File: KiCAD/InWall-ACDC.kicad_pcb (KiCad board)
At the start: 2 copper layers, 51 x 36 mm, 64 parts, among them J1 Screw_Terminal_01x02, J2 Conn_01x03, U1 HLK-PM03, U2 DS18B20

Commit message: local lib: holes 0.5, 1mm
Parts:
- REF** (x51): footprint lib_projet:hole_1mm -> Project_Module:hole_1mm
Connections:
- J2 pad 1: +3V3 -> GND
- J2 pad 3: GND -> +3V3
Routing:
- net +3V3: track 40.9 -> 34.6 mm
- net Net-(J2-Pad2): track 18.0 -> 12.1 mm
- net GND: track 59.5 -> 57.8 mm

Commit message: logo
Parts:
- added G***: LOGO, Project_Module:logo_marsu31_L5mm_H6mm, B.Cu at (173.6, 80.2)
- moved REF** 1.22 mm to (202.9, 80.9)
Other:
- board text removed: "MIT License"

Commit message: allègement logo
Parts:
- moved G*** 0.73 mm to (173.8, 80.9)

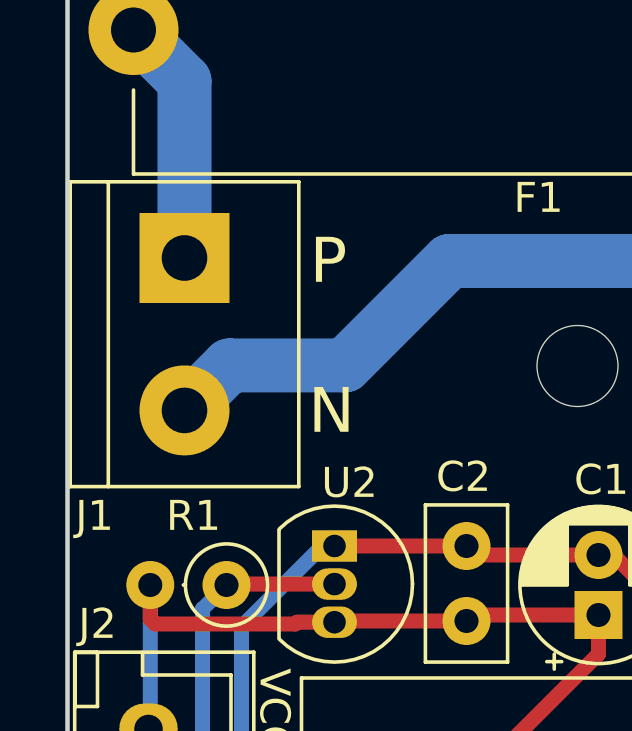
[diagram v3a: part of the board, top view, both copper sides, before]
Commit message: ajout modele 3D bornier + màj gerber
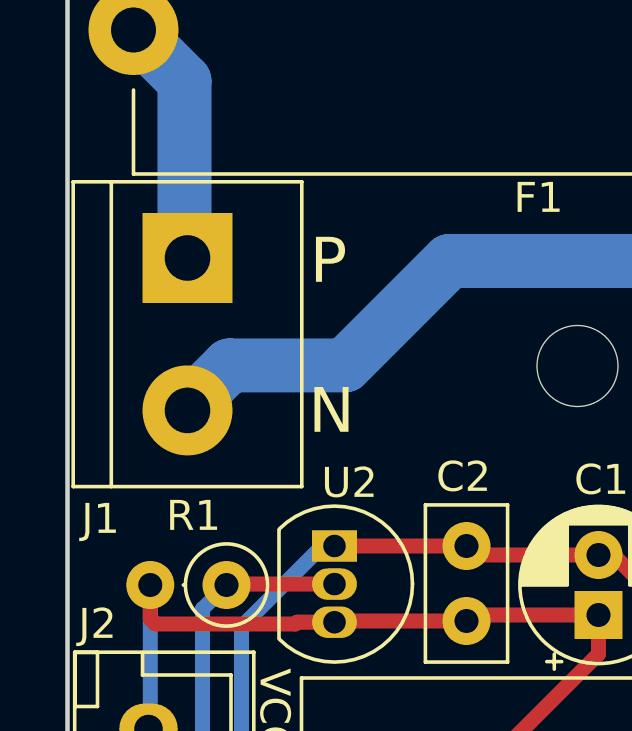
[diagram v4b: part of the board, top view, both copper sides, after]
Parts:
- J1: footprint TerminalBlock:TerminalBlock_bornier-2_P5.08mm -> Project_Module:TerminalBlock_bornier-2_P5.08mm
- moved J1 0.10 mm to (166.0, 61.4)
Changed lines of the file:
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@@
-(kicad_pcb (version 20171130) (host pcbnew 5.1.2-f72e74a~84~ubuntu18.04.1)
+(kicad_pcb (version 20171130) (host pcbnew 5.1.3-ffb9f22~84~ubuntu18.04.1)
   (general
     (thickness 1.6)
@@
       (usegerberattributes true)
       (usegerberadvancedattributes false)
-      (creategerberjobfile false)
+      (creategerberjobfile true)
       (excludeedgelayer true)
       (linewidth 0.100000)
@@
     (add_net "Net-(F1-Pad1)")
     (add_net "Net-(F1-Pad2)")
+  )
+  (module Project_Module:TerminalBlock_bornier-2_P5.08mm (layer F.Cu)
+    (at 166 61.4 270)
+    (descr "simple 2-pin terminal block, pitch 5.08mm, revamped version of bornier2")
+    (tags "terminal block bornier2")
+    (fp_text reference J1 (at 8.7 2.9 180) (layer F.SilkS)
+      (effects (font (size 1 1) (thickness 0.15)))
+    )
+    (fp_text value Screw_Terminal_01x02 (at 2.54 5.08 90) (layer F.Fab)
+      (effects (font (size 1 1) (thickness 0.15)))
+    )
+    (fp_line (start 7.79 4) (end -2.71 4) (layer F.CrtYd) (width 0.05))
+    (fp_line (start 7.79 4) (end 7.79 -4) (layer F.CrtYd) (width 0.05))
+    (fp_line (start -2.71 -4) (end -2.71 4) (layer F.CrtYd) (width 0.05))
+    (fp_line (start -2.71 -4) (end 7.79 -4) (layer F.CrtYd) (width 0.05))
+    (fp_line (start -2.54 3.81) (end 7.62 3.81) (layer F.SilkS) (width 0.12))
+    (fp_line (start -2.54 -3.81) (end -2.54 3.81) (layer F.SilkS) (width 0.12))
+    (fp_line (start 7.62 -3.81) (end -2.54 -3.81) (layer F.SilkS) (width 0.12))
+    (fp_line (start 7.62 3.81) (end 7.62 -3.81) (layer F.SilkS) (width 0.12))
+    (fp_line (start 7.62 2.54) (end -2.54 2.54) (layer F.SilkS) (width 0.12))
+    (fp_line (start 7.54 -3.75) (end -2.46 -3.75) (layer F.Fab) (width 0.1))
+    (fp_line (start 7.54 3.75) (end 7.54 -3.75) (layer F.Fab) (width 0.1))
+    (fp_line (start -2.46 3.75) (end 7.54 3.75) (layer F.Fab) (width 0.1))
+    (fp_line (start -2.46 -3.75) (end -2.46 3.75) (layer F.Fab) (width 0.1))
+    (fp_line (start -2.41 2.55) (end 7.49 2.55) (layer F.Fab) (width 0.1))
+    (fp_text user %R (at 2.54 0 90) (layer F.Fab)
+      (effects (font (size 1 1) (thickness 0.15)))
+    )
+    (pad 2 thru_hole circle (at 5.08 0 270) (size 3 3) (drill 1.52) (layers *.Cu *.Mask)
+      (net 4 NEUT))
+    (pad 1 thru_hole rect (at 0 0 270) (size 3 3) (drill 1.52) (layers *.Cu *.Mask)
+      (net 2 "Net-(F1-Pad2)"))
+    (model ${KISYS3DMOD}/TerminalBlock.3dshapes/TerminalBlock_bornier-2_P5.08mm.wrl
+      (offset (xyz 2.54 0 0))
+      (scale (xyz 1 1 1))
+      (rotate (xyz 0 0 0))
+    )
+    (model ${KIPRJMOD}/project_module.pretty/screw_terminal_01x02_P5_08mm.step
+      (offset (xyz 2.5 0 0))
+      (scale (xyz 1 1 1))
+      (rotate (xyz 0 0 -90))
+    )
   )
   (module Project_Module:logo_marsu31_L5mm_H6mm (layer B.Cu)
@@
       (scale (xyz 1 1 1))
       (rotate (xyz 0 0 0))
-    )
-  )
-  (module TerminalBlock:TerminalBlock_bornier-2_P5.08mm (layer F.Cu)
-    (at 165.9 61.4 270)
-    (descr "simple 2-pin terminal block, pitch 5.08mm, revamped version of bornier2")
-    (tags "terminal block bornier2")
-    (fp_text reference J1 (at 8.6 3 180) (layer F.SilkS)
-      (effects (font (size 1 1) (thickness 0.15)))
-    )
-    (fp_text value Screw_Terminal_01x02 (at 2.54 5.08 90) (layer F.Fab)
-      (effects (font (size 1 1) (thickness 0.15)))
-    )
-    (fp_line (start 7.79 4) (end -2.71 4) (layer F.CrtYd) (width 0.05))
-    (fp_line (start 7.79 4) (end 7.79 -4) (layer F.CrtYd) (width 0.05))
-    (fp_line (start -2.71 -4) (end -2.71 4) (layer F.CrtYd) (width 0.05))
-    (fp_line (start -2.71 -4) (end 7.79 -4) (layer F.CrtYd) (width 0.05))
-    (fp_line (start -2.54 3.81) (end 7.62 3.81) (layer F.SilkS) (width 0.12))
-    (fp_line (start -2.54 -3.81) (end -2.54 3.81) (layer F.SilkS) (width 0.12))
-    (fp_line (start 7.62 -3.81) (end -2.54 -3.81) (layer F.SilkS) (width 0.12))
-    (fp_line (start 7.62 3.81) (end 7.62 -3.81) (layer F.SilkS) (width 0.12))
-    (fp_line (start 7.62 2.54) (end -2.54 2.54) (layer F.SilkS) (width 0.12))
-    (fp_line (start 7.54 -3.75) (end -2.46 -3.75) (layer F.Fab) (width 0.1))
-    (fp_line (start 7.54 3.75) (end 7.54 -3.75) (layer F.Fab) (width 0.1))
-    (fp_line (start -2.46 3.75) (end 7.54 3.75) (layer F.Fab) (width 0.1))
-    (fp_line (start -2.46 -3.75) (end -2.46 3.75) (layer F.Fab) (width 0.1))
-    (fp_line (start -2.41 2.55) (end 7.49 2.55) (layer F.Fab) (width 0.1))
-    (fp_text user %R (at 2.54 0 90) (layer F.Fab)
-      (effects (font (size 1 1) (thickness 0.15)))
-    )
-    (pad 2 thru_hole circle (at 5.08 0 270) (size 3 3) (drill 1.52) (layers *.Cu *.Mask)
-      (net 4 NEUT))
-    (pad 1 thru_hole rect (at 0 0 270) (size 3 3) (drill 1.52) (layers *.Cu *.Mask)
-      (net 2 "Net-(F1-Pad2)"))
-    (model ${KISYS3DMOD}/TerminalBlock.3dshapes/TerminalBlock_bornier-2_P5.08mm.wrl
-      (offset (xyz 2.539999961853027 0 0))
-      (scale (xyz 1 1 1))
-      (rotate (xyz 0 0 0))
